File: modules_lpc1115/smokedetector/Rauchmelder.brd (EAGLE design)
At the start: 38 x 65 mm, 75 parts, among them IC1 BD9G101, IC2 LPC1115, Q1 BC856, Q3 BCP52, Q4 ASFL, T1 BC847C, T2 BC847C

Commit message: [RM] - removed vendor attributes from parts
attributes were not updated and thus were misleading because auf wrong c&p values. So it's better to delete them completely (and perhaps add a dedicated BOM later)
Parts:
- C15: value 4.7uF/50V -> 4.7uF 50V
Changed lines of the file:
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@@
 <attribute name="NAME" x="5.463" y="22.12" size="0.4" layer="25"/>
 <attribute name="POPULARITY" value="88" x="2.783" y="22.65" size="1.778" layer="27" display="off"/>
-<attribute name="REICHELT" value="X7R-G0805 100N" x="-21.347" y="63.29" size="1.778" layer="27" display="off"/>
 <attribute name="SPICEPREFIX" value="C" x="2.783" y="22.65" size="1.778" layer="27" display="off"/>
 <attribute name="VALUE" x="5.463" y="22.81" size="0.4" layer="27"/>
@@
 <attribute name="NAME" x="-0.2437" y="11.79" size="0.4" layer="25"/>
 <attribute name="POPULARITY" value="0" x="2.65" y="14.5113" size="1.778" layer="27" rot="R90" display="off"/>
-<attribute name="REICHELT" value="L-1616FPS 6,8µ" x="1.38" y="-37.5587" size="1.778" layer="27" rot="R90" display="off"/>
 <attribute name="SPICEPREFIX" value="L" x="2.65" y="14.5113" size="1.778" layer="27" rot="R90" display="off"/>
 <attribute name="VALUE" x="-0.2437" y="11.09" size="0.4" layer="27"/>
 </element>
-<element name="C15" library="rcl" library_urn="urn:adsk.eagle:library:334" package="C0805" package3d_urn="urn:adsk.eagle:package:23617/2" value="4.7uF/50V" x="8.13" y="13.57535" smashed="yes" rot="R270">
+<element name="C15" library="rcl" library_urn="urn:adsk.eagle:library:334" package="C0805" package3d_urn="urn:adsk.eagle:package:23617/2" value="4.7uF 50V" x="8.13" y="13.57535" smashed="yes" rot="R270">
 <attribute name="NAME" x="9.35465" y="14.2" size="0.4" layer="25"/>
 <attribute name="POPULARITY" value="88" x="8.13" y="13.57535" size="1.778" layer="27" rot="R270" display="off"/>
-<attribute name="REICHELT" value="X7R-G1206 4,7/50" x="23.37" y="32.62535" size="1.778" layer="27" rot="R270" display="off"/>
 <attribute name="SPICEPREFIX" value="C" x="8.13" y="13.57535" size="1.778" layer="27" rot="R270" display="off"/>
 <attribute name="VALUE" x="9.35465" y="13.54" size="0.4" layer="27"/>
@@
 <attribute name="NAME" x="5.413" y="20.67" size="0.4" layer="25"/>
 <attribute name="POPULARITY" value="88" x="2.783" y="20.5" size="1.778" layer="27" display="off"/>
-<attribute name="REICHELT" value="X5R-G0805 22/6" x="-36.587" y="35.74" size="1.778" layer="27" display="off"/>
 <attribute name="SPICEPREFIX" value="C" x="2.783" y="20.5" size="1.778" layer="27" display="off"/>
 <attribute name="VALUE" x="5.413" y="19.91" size="0.4" layer="27"/>
@@
 <attribute name="NAME" x="2.2" y="9.219" size="0.4" layer="25"/>
 <attribute name="POPULARITY" value="54" x="4.649" y="9.28" size="1.778" layer="27" rot="R270" display="off"/>
-<attribute name="REICHELT" value="X7R-G0805 15N" x="19.889" y="34.68" size="1.778" layer="27" rot="R270" display="off"/>
 <attribute name="SPICEPREFIX" value="C" x="4.649" y="9.28" size="1.778" layer="27" rot="R270" display="off"/>
 <attribute name="VALUE" x="2.2" y="8.359" size="0.4" layer="27"/>
@@
 <attribute name="NAME" x="9.89725" y="2.9146625" size="0.4" layer="25"/>
 <attribute name="POPULARITY" value="86" x="10.45" y="3.1774125" size="1.778" layer="27" rot="R270" display="off"/>
-<attribute name="REICHELT" value="SMD 1/4W 2,4K" x="12.99" y="50.1674125" size="1.778" layer="27" rot="R270" display="off"/>
 <attribute name="SPICEPREFIX" value="R" x="10.45" y="3.1774125" size="1.778" layer="27" rot="R270" display="off"/>
 <attribute name="VALUE" x="12.19" y="3.7419125" size="0.4" layer="27" rot="R90"/>
@@
 <attribute name="NAME" x="11.55" y="6.257" size="0.4" layer="25" rot="R90"/>
 <attribute name="POPULARITY" value="86" x="8.477" y="6.28" size="1.778" layer="27" display="off"/>
-<attribute name="REICHELT" value="SMD-0805 680" x="-44.863" y="2.47" size="1.778" layer="27" display="off"/>
 <attribute name="SPICEPREFIX" value="R" x="8.477" y="6.28" size="1.778" layer="27" display="off"/>
 <attribute name="VALUE" x="12.26" y="6.257" size="0.4" layer="27" rot="R90"/>
@@
 <attribute name="NAME" x="7.96225" y="2.9456625" size="0.4" layer="25"/>
 <attribute name="POPULARITY" value="88" x="8.396" y="3.1774125" size="1.778" layer="27" rot="R270" display="off"/>
-<attribute name="REICHELT" value="Y5R-G0603 220N" x="4.586" y="22.2274125" size="1.778" layer="27" rot="R270" display="off"/>
 <attribute name="SPICEPREFIX" value="C" x="8.396" y="3.1774125" size="1.778" layer="27" rot="R270" display="off"/>
 <attribute name="VALUE" x="7.51225" y="5.3963375" size="0.6" layer="27" display="off"/>
 </element>
 <element name="D1" library="microbuilder" package="SOD-123" value="MBRS1100" x="6.01" y="14.5113" smashed="yes" rot="R90">
-<attribute name="ALTERNATIVE#1" value="RB060M-60" x="6.01" y="14.5113" size="1.778" layer="27" rot="R90" display="off"/>
-<attribute name="ALTERNATIVE#2" value="MBRS1100" x="6.01" y="14.5113" size="1.778" layer="27" rot="R90" display="off"/>
 <attribute name="NAME" x="4.044" y="11.1113" size="0.4" layer="25" rot="R90"/>
-<attribute name="REICHELT" value="MBRS 1100 SMD" x="28.87" y="-31.2087" size="1.778" layer="27" rot="R90" display="off"/>
 <attribute name="VALUE" x="5.4113" y="17.274" size="0.4" layer="27"/>
 </element>
@@
 <attribute name="NAME" x="5.463" y="19.02" size="0.4" layer="25"/>
 <attribute name="POPULARITY" value="88" x="2.783" y="18.35" size="1.778" layer="27" display="off"/>
-<attribute name="REICHELT" value="X5R-G0805 22/6" x="2.783" y="18.35" size="1.778" layer="27" display="off"/>
 <attribute name="SPICEPREFIX" value="C" x="2.783" y="18.35" size="1.778" layer="27" display="off"/>
 <attribute name="VALUE" x="5.463" y="18.26" size="0.4" layer="27"/>

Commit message: [RM] - optimized silkscreen
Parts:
- C9: value 330µ -> 330uF
- moved T2 0.50 mm to (26.7, 38.9)
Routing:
- net N$8: track 17.0 -> 16.5 mm
- net N$7: track 4.31 -> 3.81 mm
- net GND: track 48.9 -> 49.0 mm, vias 91 -> 98
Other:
- board text removed: "C21 = 270n"

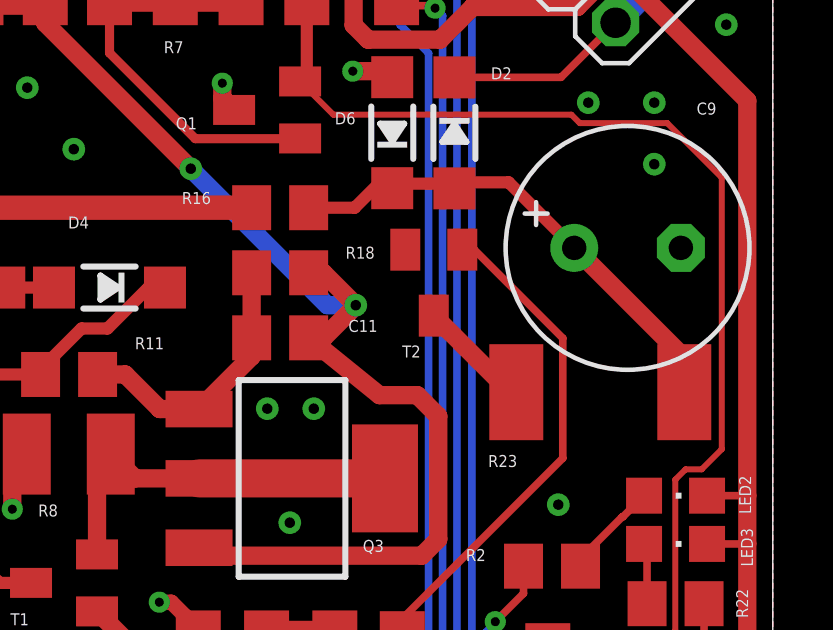
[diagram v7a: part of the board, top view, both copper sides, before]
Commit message: [RM] - changed T2 from BC847 to BC817
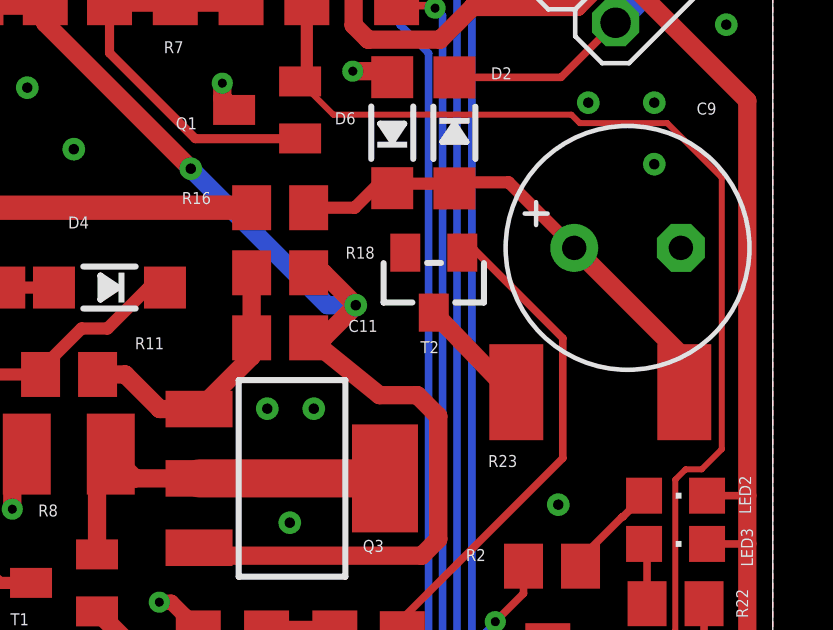
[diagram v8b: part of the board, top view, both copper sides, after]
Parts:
- T2: value BC847C -> BC817; device transistor:SOT23 -> microbuilder:SOT23-WIDE
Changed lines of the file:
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@@
 <attribute name="VALUE" x="37.74" y="27.721225" size="0.4" layer="27" rot="R90"/>
 </element>
-<element name="T2" library="transistor" package="SOT23" value="BC847C" x="26.7" y="38.9" smashed="yes" rot="R180">
-<attribute name="NAME" x="25.645" y="36.405" size="0.4" layer="25"/>
-<attribute name="VALUE" x="25.645" y="35.775" size="0.4" layer="27"/>
+<element name="T2" library="microbuilder" package="SOT23-WIDE" value="BC817" x="26.7" y="38.9" smashed="yes" rot="R180">
+<attribute name="NAME" x="26.255" y="36.55" size="0.4" layer="25" ratio="18"/>
+<attribute name="VALUE" x="26.255" y="35.915" size="0.4064" layer="27" ratio="10"/>
 </element>
 <element name="R23" library="rcl" library_urn="urn:adsk.eagle:library:334" package="R2512" package3d_urn="urn:adsk.eagle:package:23545/2" value="220R" x="32.25" y="35.25" smashed="yes" rot="R180">
@@
 <wire x1="13.02335" y1="17.197615625" x2="13.02335" y2="15.0502375" width="0" layer="19" extent="1-1"/>
 <wire x1="14.632" y1="8.74255" x2="12.1" y2="11.65" width="0" layer="19" extent="1-1"/>
-<wire x1="11.6" y1="21.9" x2="7.4" y2="21.85" width="0" layer="19" extent="1-1"/>
-<wire x1="11.6" y1="24.45" x2="11.6" y2="21.9" width="0" layer="19" extent="1-1"/>
+<wire x1="11.6" y1="24.45" x2="7.4" y2="24.5" width="0" layer="19" extent="1-1"/>
+<wire x1="11.6" y1="21.9" x2="11.6" y2="24.45" width="0" layer="19" extent="1-1"/>
 <wire x1="14.8" y1="24.45" x2="11.6" y2="24.45" width="0" layer="19" extent="1-1"/>
 <wire x1="14.8" y1="22.25" x2="14.8" y2="24.45" width="0" layer="19" extent="1-1"/>
@@
 <wire x1="22.083125" y1="7.2072875" x2="21.6666" y2="12.2436" width="0" layer="19" extent="1-1"/>
 <wire x1="24.260625" y1="7.2072875" x2="22.083125" y2="7.2072875" width="0" layer="19" extent="1-1"/>
-<wire x1="25.75" y1="40" x2="25.315" y2="45.75" width="0" layer="19" extent="1-1"/>
+<wire x1="25.75" y1="39.9" x2="25.315" y2="45.75" width="0" layer="19" extent="1-1"/>
 <wire x1="14.632" y1="2.24015" x2="14.632" y2="8.74255" width="0" layer="19" extent="1-1"/>
 <wire x1="30.4" y1="1.8" x2="30.793125" y2="9.1072875" width="0" layer="19" extent="1-1"/>
@@
 <contactref element="T2" pad="3"/>
 <wire x1="29.45" y1="35.25" x2="29.25" y2="35.25" width="0.6096" layer="1"/>
-<wire x1="29.25" y1="35.25" x2="26.7" y2="37.8" width="0.6096" layer="1"/>
+<wire x1="29.25" y1="35.25" x2="26.7" y2="37.9" width="0.6096" layer="1"/>
 </signal>
 <signal name="N$8">
@@
 <contactref element="R24" pad="1"/>
 <wire x1="25.65" y1="27.7" x2="25.65" y2="27.3" width="0.254" layer="1"/>
-<wire x1="27.65" y1="40" x2="28.05" y2="40" width="0.254" layer="1"/>
+<wire x1="27.65" y1="39.9" x2="28.05" y2="40" width="0.254" layer="1"/>
 <wire x1="28.05" y1="40" x2="31" y2="37.05" width="0.254" layer="1"/>
 <wire x1="31" y1="37.05" x2="31" y2="33.05" width="0.254" layer="1"/>
